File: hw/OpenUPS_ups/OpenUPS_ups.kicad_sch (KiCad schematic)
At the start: 24 parts, among them J101 Barrel Jack, J102 XT30PW-M, J103 XT30PW-M, J104 S2B-PH-K_1x02, J105 S2B-PH-K_1x02, J106 Screw Terminal, J107 Screw Terminal, J108 Screw Terminal, J109 JST XH, J110 JST XH, U101 AVR32DB48x-xPT

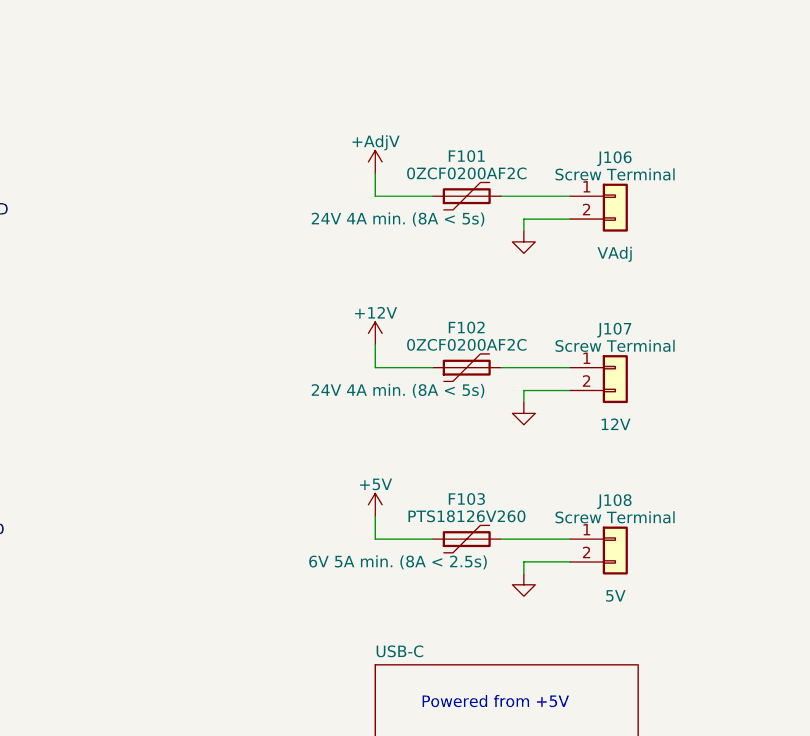
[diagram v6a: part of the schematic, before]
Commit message: Replaced polyfuses with 1206 fuses #12
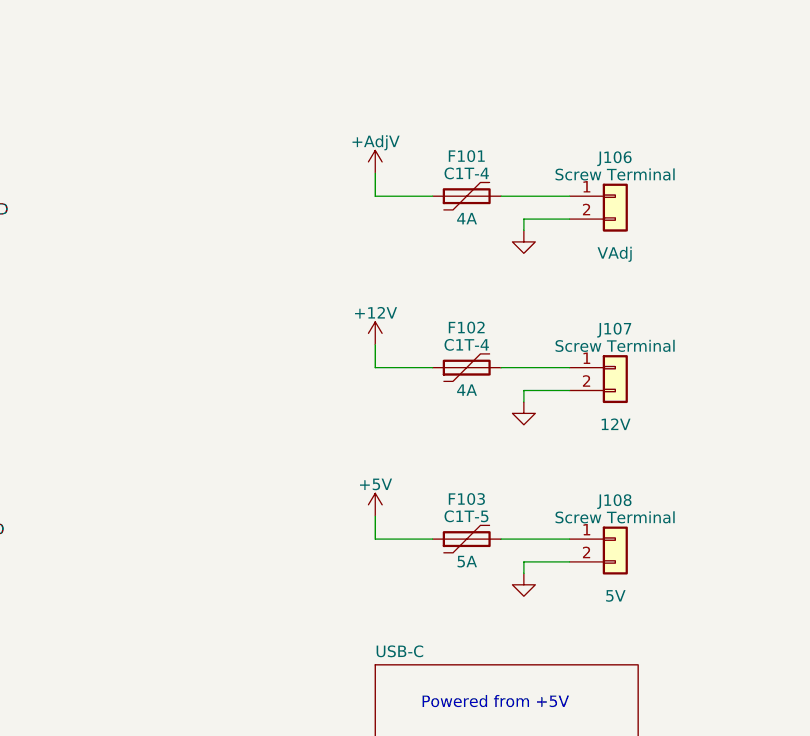
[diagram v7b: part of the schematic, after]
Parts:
- F101, F102: value 0ZCF0200AF2C -> C1T-4; footprint Fuse:Fuse_2920_7451Metric -> Fuse:Fuse_1206_3216Metric; Comment 24V 4A min. (8A < 5s) -> 4A
- F103: value PTS18126V260 -> C1T-5; footprint Fuse:Fuse_1812_4532Metric -> Fuse:Fuse_1206_3216Metric; Comment 6V 5A min. (8A < 2.5s) -> 5A
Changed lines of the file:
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@@
-    )
-  )
-  (symbol (lib_id "Device:Polyfuse") (at 295.91 66.04 90) (unit 1)
-    (in_bom yes) (on_board yes) (dnp no)
-    (property "Reference" "F102" (at 295.91 61.6331 90)
-      (effects (font (size 1.27 1.27)))
-    )
-    (property "Value" "0ZCF0200AF2C" (at 295.91 63.5541 90)
-      (effects (font (size 1.27 1.27)))
-    )
-    (property "Footprint" "Fuse:Fuse_2920_7451Metric" (at 300.99 64.77 0)
-      (effects (font (size 1.27 1.27)) (justify left) hide)
-    )
-    (property "Datasheet" "https://www.mouser.pl/datasheet/2/87/eaton_pts1812_6_60_volt_dc_surface_mount_resettabl-1608747.pdf" (at 295.91 66.04 0)
-      (effects (font (size 1.27 1.27)) hide)
-    )
-    (property "Comment" "24V 4A min. (8A < 5s)" (at 288.29 68.58 90)
-      (effects (font (size 1.27 1.27)))
-    )
-    (pin "1")
-    (pin "2")
-    (instances
-      (project "OpenUPS_ups"
-        (path "/f77faec3-eac4-47f3-a2de-ec4a039f4502"
-          (reference "F102") (unit 1)
-        )
-      )
     )
   )
@@
     )
   )
+  (symbol (lib_id "Device:Polyfuse") (at 295.91 46.99 90) (unit 1)
+    (in_bom yes) (on_board yes) (dnp no)
+    (property "Reference" "F101" (at 295.91 42.5831 90)
+      (effects (font (size 1.27 1.27)))
+    )
+    (property "Value" "C1T-4" (at 295.91 44.5041 90)
+      (effects (font (size 1.27 1.27)))
+    )
+    (property "Footprint" "Fuse:Fuse_1206_3216Metric" (at 300.99 45.72 0)
+      (effects (font (size 1.27 1.27)) (justify left) hide)
+    )
+    (property "Datasheet" "" (at 295.91 46.99 0)
+      (effects (font (size 1.27 1.27)) hide)
+    )
+    (property "Comment" "4A" (at 295.91 49.53 90)
+      (effects (font (size 1.27 1.27)))
+    )
+    (property "Field5" "" (at 295.91 46.99 90)
+      (effects (font (size 1.27 1.27)) hide)
+    )
+    (pin "1")
+    (pin "2")
+    (instances
+      (project "OpenUPS_ups"
+        (path "/f77faec3-eac4-47f3-a2de-ec4a039f4502"
+          (reference "F101") (unit 1)
+        )
+      )
+    )
+  )
   (symbol (lib_id "Connector_Generic:Conn_01x02") (at 133.35 68.58 0) (unit 1)
     (in_bom yes) (on_board yes) (dnp no) (fields_autoplaced)
@@
         (path "/f77faec3-eac4-47f3-a2de-ec4a039f4502"
           (reference "#PWR0102") (unit 1)
+        )
+      )
+    )
+  )
+  (symbol (lib_id "Device:Polyfuse") (at 295.91 66.04 90) (unit 1)
+    (in_bom yes) (on_board yes) (dnp no)
+    (property "Reference" "F102" (at 295.91 61.6331 90)
+      (effects (font (size 1.27 1.27)))
+    )
+    (property "Value" "C1T-4" (at 295.91 63.5541 90)
+      (effects (font (size 1.27 1.27)))
+    )
+    (property "Footprint" "Fuse:Fuse_1206_3216Metric" (at 300.99 64.77 0)
+      (effects (font (size 1.27 1.27)) (justify left) hide)
+    )
+    (property "Datasheet" "" (at 295.91 66.04 0)
+      (effects (font (size 1.27 1.27)) hide)
+    )
+    (property "Comment" "4A" (at 295.91 68.58 90)
+      (effects (font (size 1.27 1.27)))
+    )
+    (property "Field5" "" (at 295.91 66.04 90)
+      (effects (font (size 1.27 1.27)) hide)
+    )
+    (pin "1")
+    (pin "2")
+    (instances
+      (project "OpenUPS_ups"
+        (path "/f77faec3-eac4-47f3-a2de-ec4a039f4502"
+          (reference "F102") (unit 1)
         )
       )
@@
       (effects (font (size 1.27 1.27)))
     )
-    (property "Value" "PTS18126V260" (at 295.91 82.6041 90)
-      (effects (font (size 1.27 1.27)))
-    )
-    (property "Footprint" "Fuse:Fuse_1812_4532Metric" (at 300.99 83.82 0)
+    (property "Value" "C1T-5" (at 295.91 82.6041 90)
+      (effects (font (size 1.27 1.27)))
+    )
+    (property "Footprint" "Fuse:Fuse_1206_3216Metric" (at 300.99 83.82 0)
       (effects (font (size 1.27 1.27)) (justify left) hide)
     )
-    (property "Datasheet" "https://www.mouser.pl/datasheet/2/87/eaton_pts1812_6_60_volt_dc_surface_mount_resettabl-1608747.pdf" (at 295.91 85.09 0)
-      (effects (font (size 1.27 1.27)) hide)
-    )
-    (property "Comment" "6V 5A min. (8A < 2.5s)" (at 288.29 87.63 90)
+    (property "Datasheet" "" (at 295.91 85.09 0)
+      (effects (font (size 1.27 1.27)) hide)
+    )
+    (property "Comment" "5A" (at 295.91 87.63 90)
       (effects (font (size 1.27 1.27)))
     )
@@
         )
       )
-    )
-  )
-  (symbol (lib_id "Device:Polyfuse") (at 295.91 46.99 90) (unit 1)
-    (in_bom yes) (on_board yes) (dnp no)
-    (property "Reference" "F101" (at 295.91 42.5831 90)
-      (effects (font (size 1.27 1.27)))
-    )
-    (property "Value" "0ZCF0200AF2C" (at 295.91 44.5041 90)
-      (effects (font (size 1.27 1.27)))
-    )
-    (property "Footprint" "Fuse:Fuse_2920_7451Metric" (at 300.99 45.72 0)
-      (effects (font (size 1.27 1.27)) (justify left) hide)
-    )
-    (property "Datasheet" "https://www.mouser.pl/datasheet/2/87/eaton_pts1812_6_60_volt_dc_surface_mount_resettabl-1608747.pdf" (at 295.91 46.99 0)
-      (effects (font (size 1.27 1.27)) hide)
-    )
-    (property "Comment" "24V 4A min. (8A < 5s)" (at 288.29 49.53 90)
-      (effects (font (size 1.27 1.27)))
-    )
-    (pin "1")
-    (pin "2")
-    (instances
-      (project "OpenUPS_ups"
-        (path "/f77faec3-eac4-47f3-a2de-ec4a039f4502"
-          (reference "F101") (unit 1)
-        )
-      )

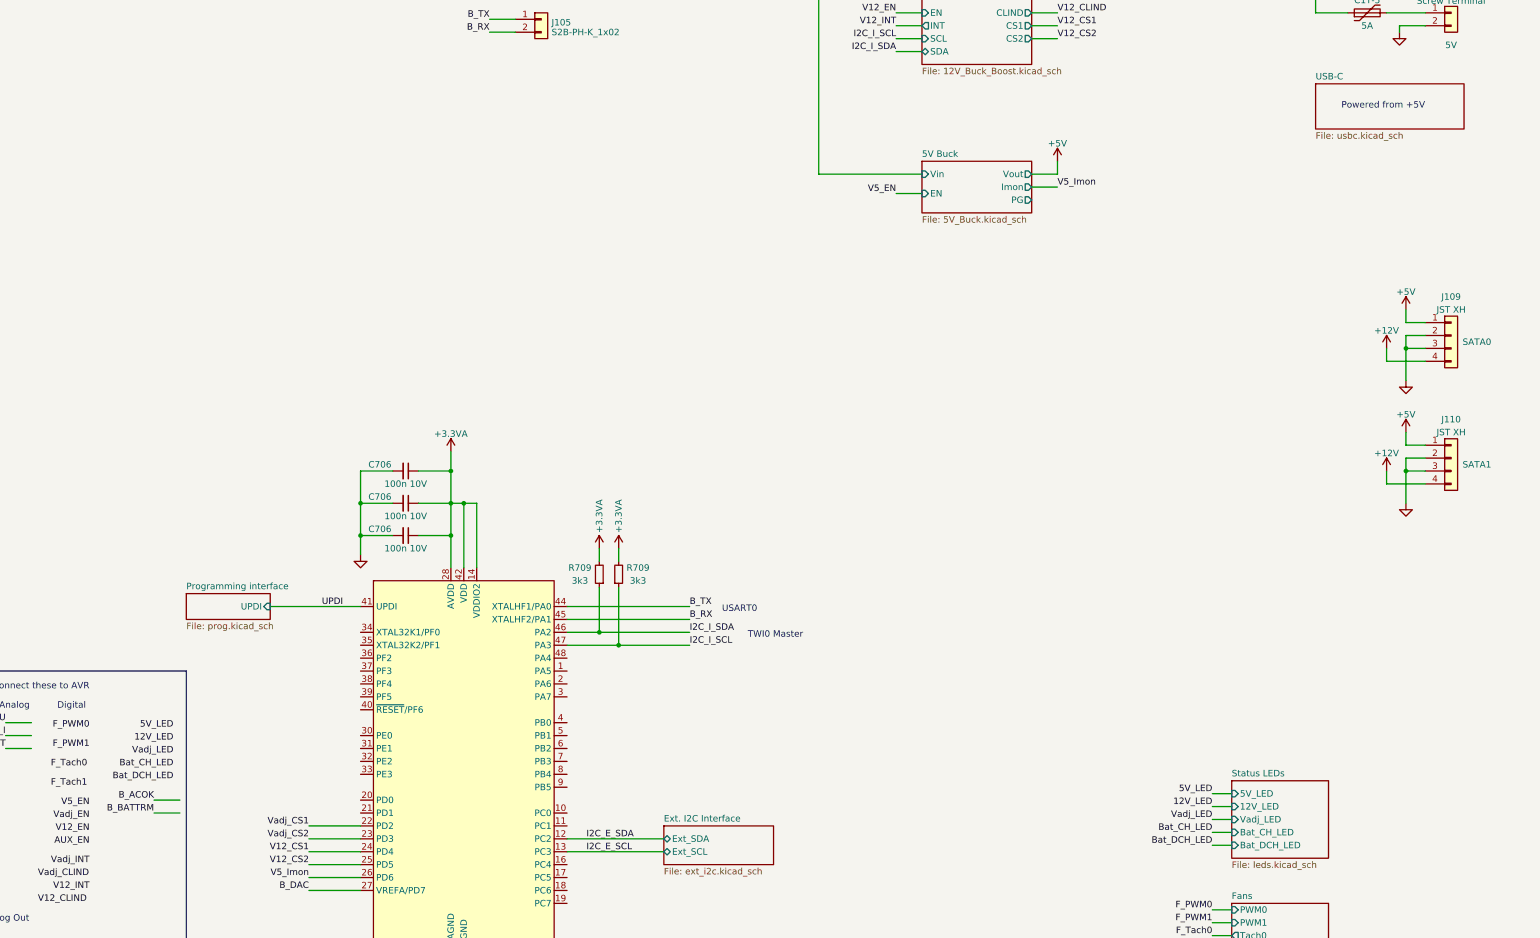
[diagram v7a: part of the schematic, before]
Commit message: Issue #30: USB Force ON feature
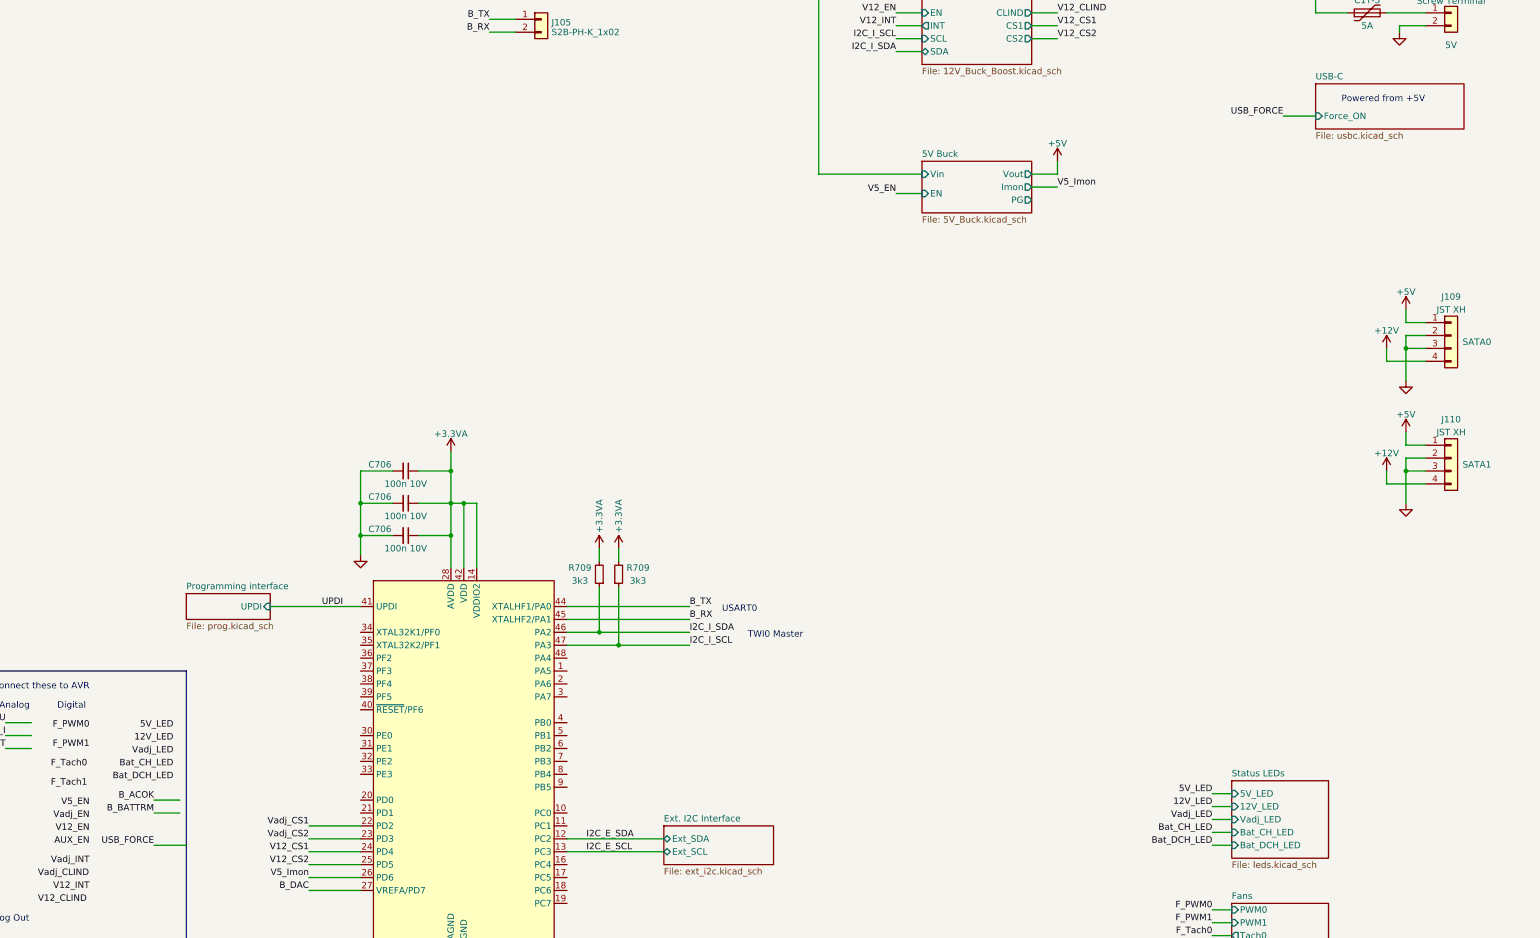
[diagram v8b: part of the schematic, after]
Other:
- sheet USB-C ports: added Force_ON; removed none
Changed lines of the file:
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@@
+    (stroke (width 0) (type default))
+  )
+  (wire (pts (xy 57.15 248.92) (xy 63.5 248.92))
     (stroke (width 0) (type default))
   )
@@
   )
   (wire (pts (xy 234.95 45.72) (xy 229.87 45.72))
+    (stroke (width 0) (type default))
+  )
+  (wire (pts (xy 279.4 105.41) (xy 285.75 105.41))
     (stroke (width 0) (type default))
   )
@@
     (effects (font (size 1.27 1.27)) (justify left bottom))
   )
-  (text "Powered from +5V" (at 290.83 104.14 0)
+  (text "Powered from +5V" (at 290.83 102.87 0)
     (effects (font (size 1.27 1.27)) (justify left bottom))
   )
@@
     (effects (font (size 1.27 1.27)) (justify right bottom))
   )
+  (label "USB_FORCE" (at 57.15 248.92 180) (fields_autoplaced)
+    (effects (font (size 1.27 1.27)) (justify right bottom))
+  )
   (label "V12_CLIND" (at 34.29 260.35 0) (fields_autoplaced)
     (effects (font (size 1.27 1.27)) (justify left bottom))
   )
   (label "Vadj_LED" (at 60.96 231.14 180) (fields_autoplaced)
+    (effects (font (size 1.27 1.27)) (justify right bottom))
+  )
+  (label "USB_FORCE" (at 279.4 105.41 180) (fields_autoplaced)
     (effects (font (size 1.27 1.27)) (justify right bottom))
   )
@@
       (effects (font (size 1.27 1.27)) (justify left top))
     )
-    (instances
+    (pin "Force_ON" input (at 285.75 105.41 180)
+      (effects (font (size 1.27 1.27)) (justify left))
+    )
+    (instances
